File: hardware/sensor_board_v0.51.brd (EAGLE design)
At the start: 46.8 x 39.9 mm, 47 parts, among them IC1 BMP280, J3 USB-MICROB, U1 ATMEGA328P, U2 TSL2561, U5 FT231XS, U6 ADMP401, U7 SHT31-DIS, U8 MCP1703CB, U9 MCP1703CB, Y1 16MHZ

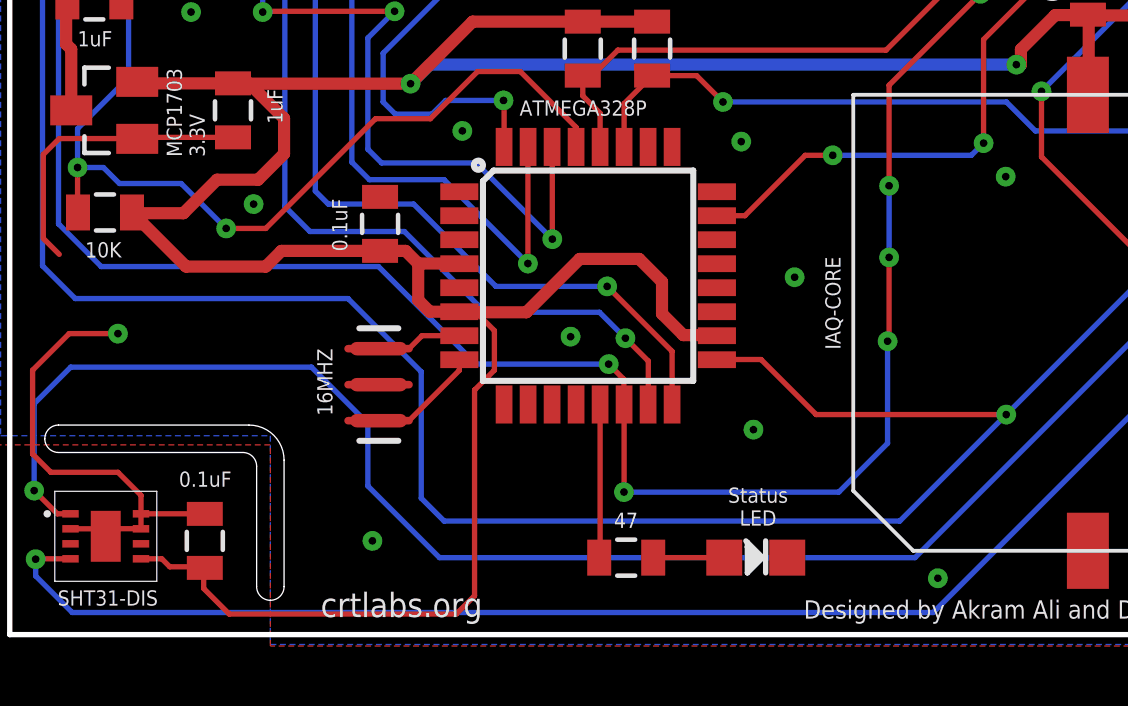
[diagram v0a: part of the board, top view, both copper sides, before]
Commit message: Adjusted one via to align with the 'o' of 'Board'
because ¯\_(ツ)_/¯
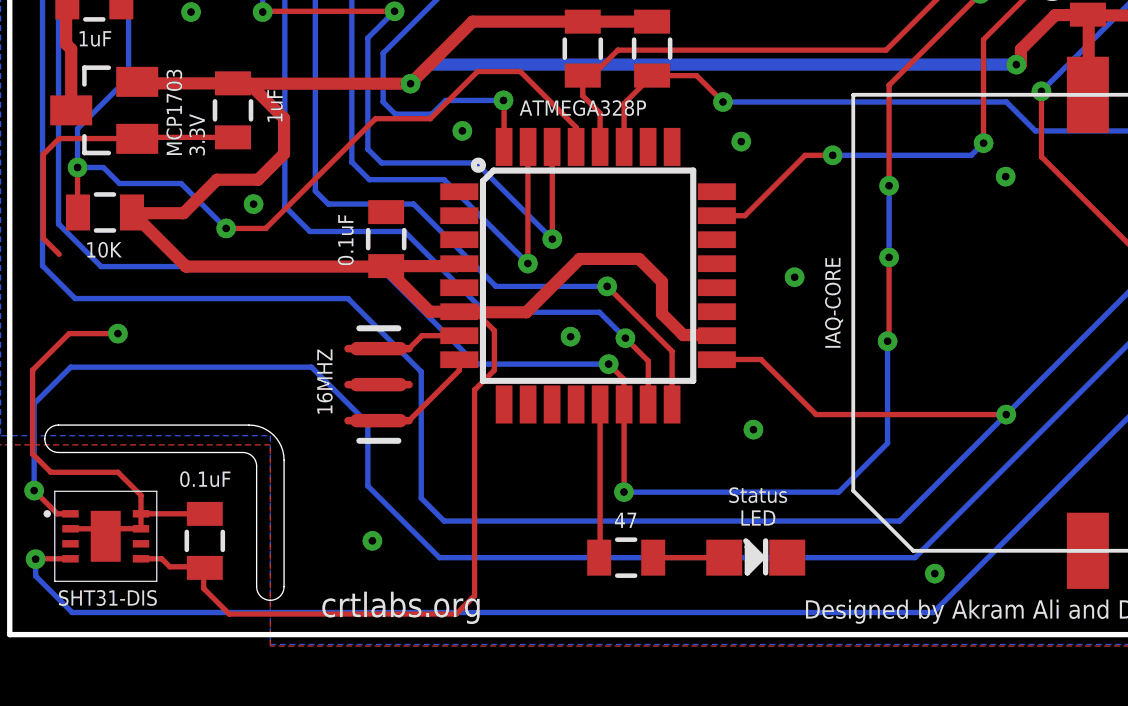
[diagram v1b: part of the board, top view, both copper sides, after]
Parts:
- moved C15 0.55 mm to (18.4, 19.8)
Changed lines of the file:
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@@
 <attribute name="VALUE" x="47.1932" y="50.3936" size="0.8128" layer="27" ratio="10"/>
 </element>
-<element name="C15" library="SparkFun-Passives" package="0805" value="0.1uF" x="18.2372" y="20.32" smashed="yes" rot="R90">
-<attribute name="VALUE" x="17.145" y="19.4056" size="0.508" layer="121" font="vector" rot="R90"/>
+<element name="C15" library="SparkFun-Passives" package="0805" value="0.1uF" x="18.4404" y="19.812" smashed="yes" rot="R90">
+<attribute name="VALUE" x="17.3482" y="18.8976" size="0.508" layer="121" font="vector" rot="R90"/>
 </element>
 <element name="IC1" library="bosch-bmp280" package="BMP280" value="BMP280" x="35.7632" y="33.782" smashed="yes" rot="R90">
@@
 <contactref element="U7" pad="P$7"/>
 <contactref element="U7" pad="P$2"/>
-<via x="36.83" y="8.509" extent="1-16" drill="0.254" diameter="0.127"/>
+<via x="36.7284" y="8.6614" extent="1-16" drill="0.254" diameter="0.127"/>
 <via x="39.0906" y="21.8948" extent="1-16" drill="0.254" diameter="0.127"/>
 <via x="47.5742" y="35.7124" extent="1-16" drill="0.254" diameter="0.127"/>
@@
 <wire x1="34.8078" y1="34.757" x2="34.9632" y2="34.757" width="0.4064" layer="1"/>
 <wire x1="27.305" y1="27.062" x2="24.9936" y2="27.062" width="0.4064" layer="1"/>
-<wire x1="18.2372" y1="19.42" x2="19.0864" y2="19.42" width="0.4064" layer="1"/>
-<wire x1="19.0864" y1="19.42" x2="19.5072" y2="18.9992" width="0.4064" layer="1"/>
-<wire x1="19.5072" y1="18.9992" x2="20.8724" y2="18.9992" width="0.4064" layer="1"/>
 <wire x1="20.8724" y1="18.9992" x2="20.8788" y2="18.9928" width="0.4064" layer="1"/>
 <wire x1="20.8788" y1="17.3928" x2="19.8944" y2="17.3928" width="0.4064" layer="1"/>
-<wire x1="19.8944" y1="17.3928" x2="19.5072" y2="17.78" width="0.4064" layer="1"/>
-<wire x1="19.5072" y1="17.78" x2="19.5072" y2="18.9992" width="0.4064" layer="1"/>
-<wire x1="18.2372" y1="19.42" x2="14.9496" y2="19.42" width="0.4064" layer="1"/>
 <wire x1="49.2396" y1="32.0294" x2="49.2396" y2="28.2448" width="0.4064" layer="1"/>
 <wire x1="10.2682" y1="9.156" x2="10.9608" y2="9.156" width="0.1778" layer="1"/>
@@
 <wire x1="22.0472" y1="16.764" x2="21.4376" y2="17.3736" width="0.1778" layer="1"/>
 <wire x1="19.8882" y1="25.6286" x2="39.4462" y2="25.6286" width="0.4064" layer="16"/>
-<wire x1="14.9496" y1="19.42" x2="14.4272" y2="18.8976" width="0.4064" layer="1"/>
-<wire x1="14.4272" y1="18.8976" x2="11.7712" y2="18.8976" width="0.4064" layer="1"/>
 <wire x1="11.7712" y1="18.8976" x2="9.9678" y2="20.701" width="0.4064" layer="1"/>
 <wire x1="19.8882" y1="25.6286" x2="19.2532" y2="24.9936" width="0.4064" layer="16"/>
@@
 <wire x1="41.8592" y1="27.2686" x2="41.8338" y2="27.294" width="0.4064" layer="1"/>
 <wire x1="41.8592" y1="27.2686" x2="48.2634" y2="27.2686" width="0.4064" layer="1"/>
+<wire x1="11.7712" y1="18.8976" x2="18.426" y2="18.8976" width="0.4064" layer="1"/>
+<wire x1="18.426" y1="18.8976" x2="18.4404" y2="18.912" width="0.4064" layer="1"/>
+<wire x1="19.8944" y1="17.3928" x2="18.4404" y2="18.8468" width="0.4064" layer="1"/>
+<wire x1="18.4404" y1="18.8468" x2="18.4404" y2="18.912" width="0.4064" layer="1"/>
+<wire x1="20.8788" y1="18.9928" x2="20.798" y2="18.912" width="0.4064" layer="1"/>
+<wire x1="20.798" y1="18.912" x2="18.4404" y2="18.912" width="0.4064" layer="1"/>
 </signal>
 <signal name="SCL">
